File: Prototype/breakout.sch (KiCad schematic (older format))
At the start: 8 parts, among them J2 Conn_02x03_Counter_Clockwise, Q1 BSC026NE2LS5, U1 INA214, U2 bq297xx, U3 LM21215, U4 TPS61088, U5 ADA4891-4

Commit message: Test
hello
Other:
- note added: "hello"
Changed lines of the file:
@@
 Wire Wire Line
 	1700 4100 1900 4100
+Text Notes 1700 4800 0    60   ~ 0
+hello
 $EndSCHEMATC

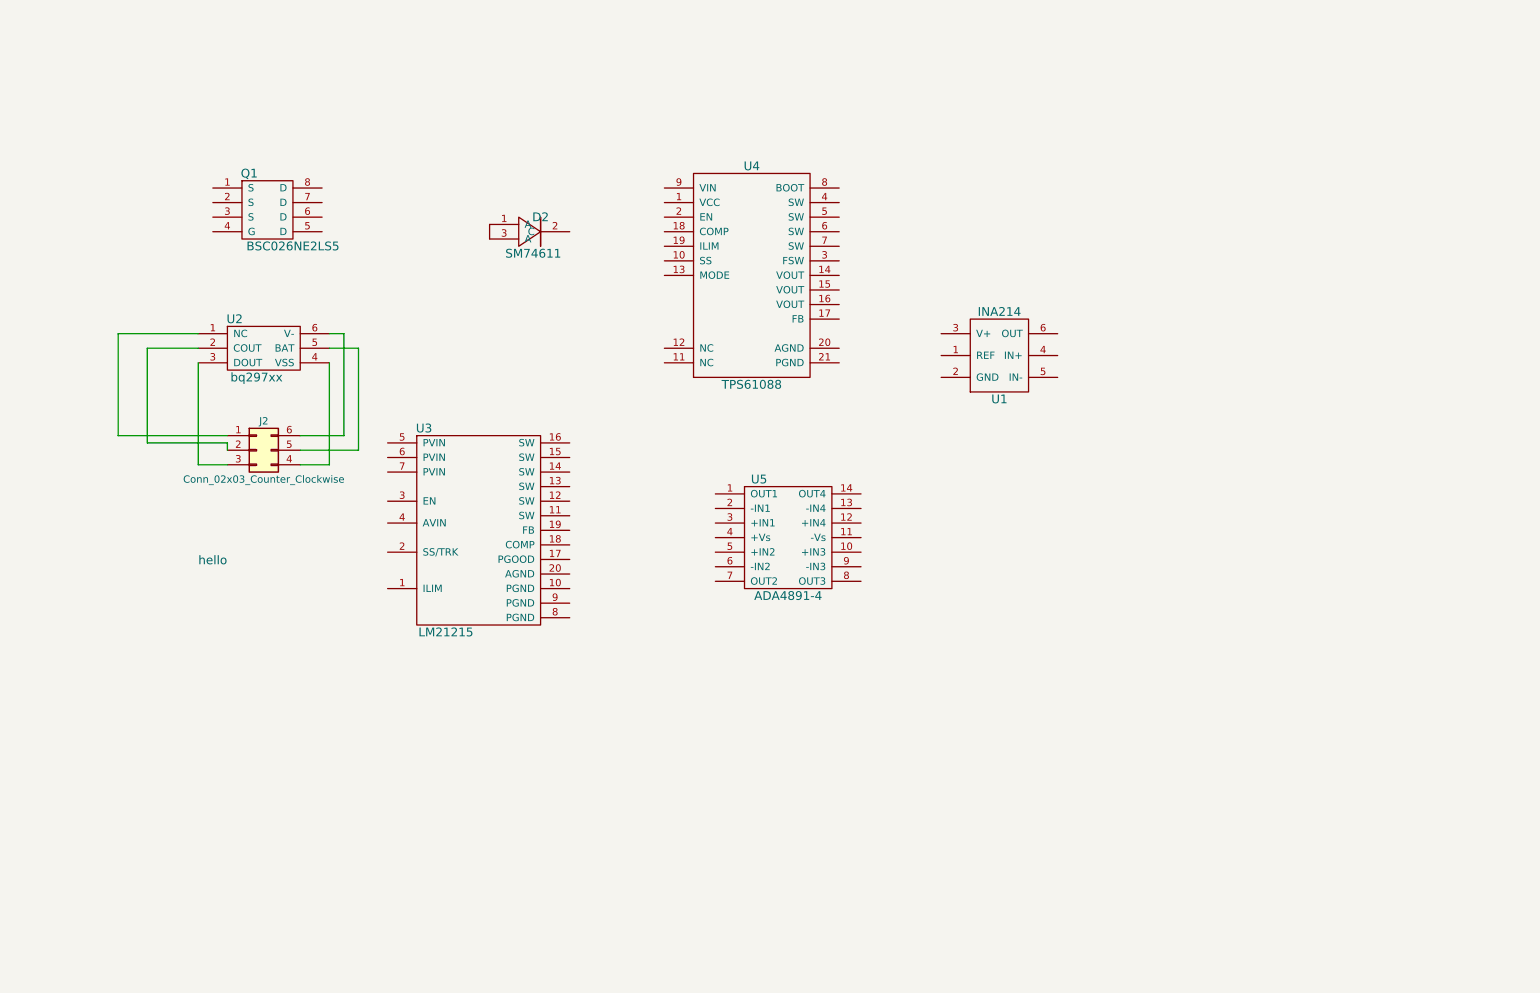
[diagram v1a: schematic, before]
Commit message: Finished laying out breakout boards
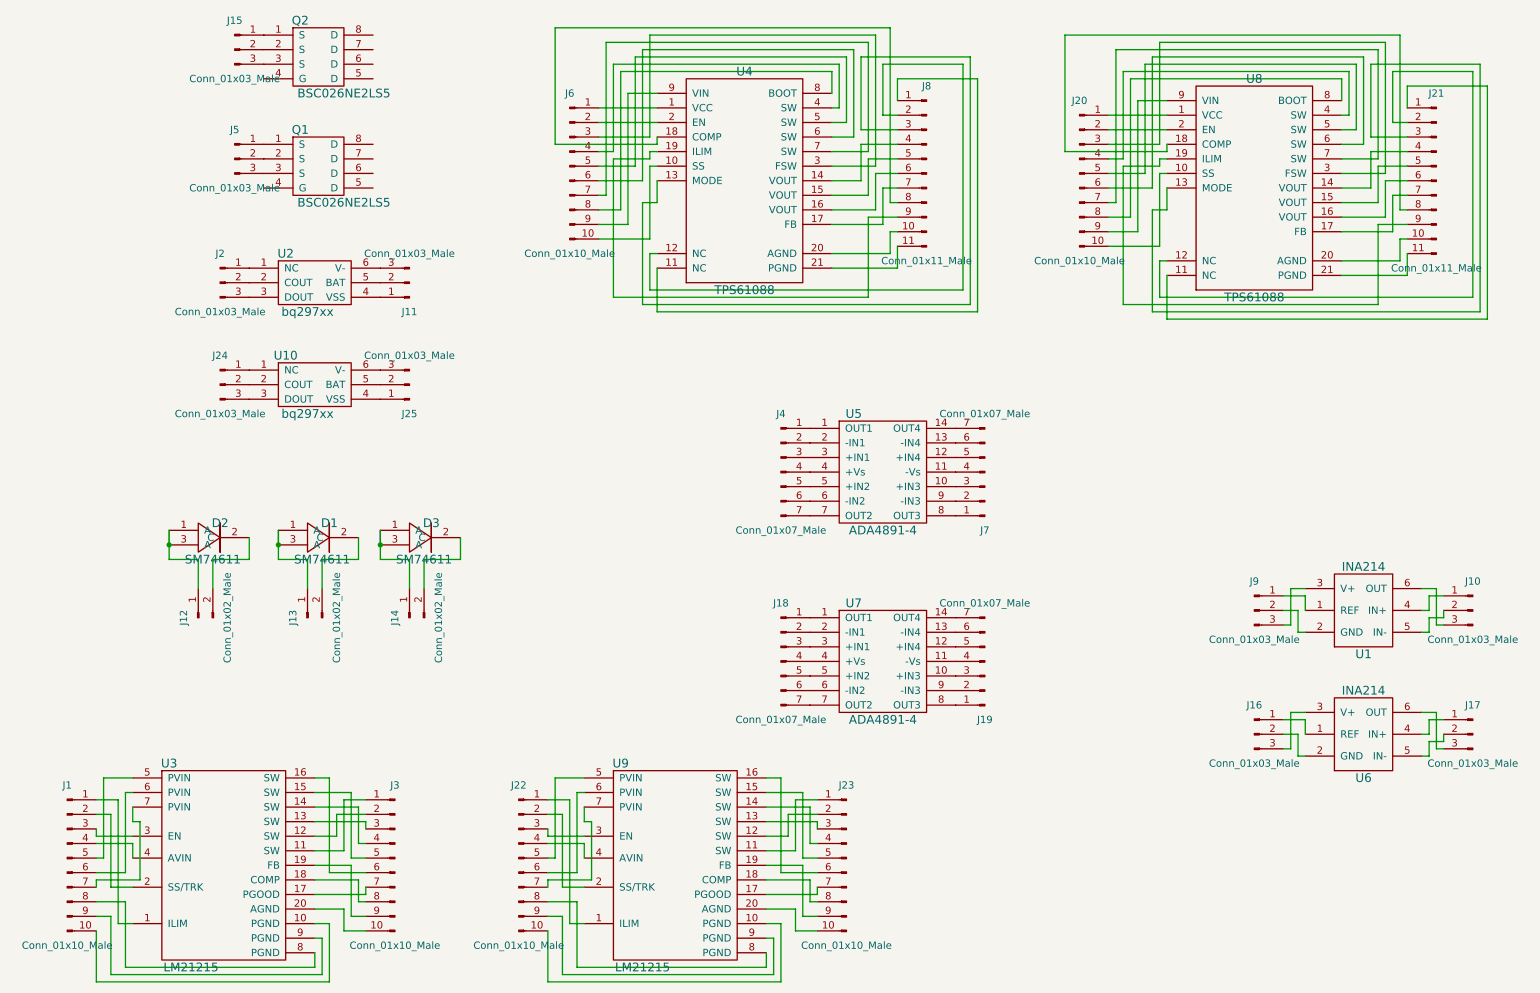
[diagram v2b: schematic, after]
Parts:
- removed J2: Conn_02x03_Counter_Clockwise, Pin_Headers:Pin_Header_Straight_2x03_Pitch2.54mm, symbol Conn_02x03_Counter_Clockwise
- added D1, D3: SM74611, Diodes_SMD:DD-PAK_TO263_SingleDiode, symbol SM74611
- added J1, J20, J22, J23, J3, J6: Conn_01x10_Male, Pin_Headers:Pin_Header_Straight_1x10_Pitch2.54mm, symbol Conn_01x10_Male
- added J10, J11, J15, J16, J17, J2, J24, J25, J5, J9: Conn_01x03_Male, Pin_Headers:Pin_Header_Straight_1x03_Pitch2.54mm, symbol Conn_01x03_Male
- added J12, J13, J14: Conn_01x02_Male, Pin_Headers:Pin_Header_Straight_1x02_Pitch2.54mm, symbol Conn_01x02_Male
- added J18, J19, J4, J7: Conn_01x07_Male, Pin_Headers:Pin_Header_Straight_1x07_Pitch2.54mm, symbol Conn_01x07_Male
- added J21, J8: Conn_01x11_Male, Pin_Headers:Pin_Header_Straight_1x11_Pitch2.54mm, symbol Conn_01x11_Male
- added Q2: BSC026NE2LS5, Housings_SON:VSONP-8-1EP_5x6_Pitch1.27mm, symbol BSC026NE2LS5
- added U10: bq297xx, Housings_SON:WSON6_1.5x1.5mm_Pitch0.5mm, symbol bq297xx
- added U6: INA214, kicad-libraries:SC70-6, symbol INA214
- added U7: ADA4891-4, SMD_Packages:SSOP-14, symbol ADA4891-4
- added U8: TPS61088, Housings_DFN_QFN:Texas_VQFN-RGR-20, symbol TPS61088
- added U9: LM21215, SMD_Packages:SSOP-20, symbol LM21215
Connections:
- net at U1.1 (REF): now also J9.1 (Pin_1)
- net at U1.2 (GND): now also J9.2 (Pin_2)
- net at U1.3 (V+): now also J9.3 (Pin_3)
- net at U1.4 (IN+): now also J10.1 (Pin_1)
- net at U1.5 (IN-): now also J10.2 (Pin_2)
- net at U1.6 (OUT): now also J10.3 (Pin_3)
- net at D2.1 (A): now also D2.3 (A), J12.1 (Pin_1)
- net at D2.2 (C): now also J12.2 (Pin_2)
- net at U4.1 (VCC): now also J6.1 (Pin_1)
- net at U4.10 (SS): now also J6.10 (Pin_10)
- net at U4.11 (NC): now also J8.1 (Pin_1)
- net at U4.12 (NC): now also J8.2 (Pin_2)
- net at U4.13 (MODE): now also J8.3 (Pin_3)
- net at U4.14 (VOUT): now also J8.4 (Pin_4)
- net at U4.15 (VOUT): now also J8.5 (Pin_5)
- net at U4.16 (VOUT): now also J8.6 (Pin_6)
- net at U4.17 (FB): now also J8.7 (Pin_7)
- net at U4.18 (COMP): now also J8.8 (Pin_8)
- net at U4.19 (ILIM): now also J8.9 (Pin_9)
- net at U4.2 (EN): now also J6.2 (Pin_2)
- net at U4.20 (AGND): now also J8.10 (Pin_10)
- net at U4.21 (PGND): now also J8.11 (Pin_11)
- net at U4.3 (FSW): now also J6.3 (Pin_3)
- net at U4.4 (SW): now also J6.4 (Pin_4)
- net at U4.5 (SW): now also J6.5 (Pin_5)
- net at U4.6 (SW): now also J6.6 (Pin_6)
- net at U4.7 (SW): now also J6.7 (Pin_7)
- net at U4.8 (BOOT): now also J6.8 (Pin_8)
- net at U4.9 (VIN): now also J6.9 (Pin_9)
- net at Q1.1 (S): now also J5.1 (Pin_1)
- net at Q1.2 (S): now also J5.2 (Pin_2)
- net at Q1.3 (S): now also J5.3 (Pin_3)
- net at U2.1 (NC): now also J2.1 (Pin_1)
- net at U2.2 (COUT): now also J2.2 (Pin_2)
- net at U2.3 (DOUT): now also J2.3 (Pin_3)
- net at U2.4 (VSS): now also J11.1 (Pin_1)
- net at U2.5 (BAT): now also J11.2 (Pin_2)
- net at U2.6 (V-): now also J11.3 (Pin_3)
- net at U3.1 (ILIM): now also J1.1 (Pin_1)
- net at U3.10 (PGND): now also J1.10 (Pin_10)
- net at U3.11 (SW): now also J3.1 (Pin_1)
- net at U3.12 (SW): now also J3.2 (Pin_2)
- net at U3.13 (SW): now also J3.3 (Pin_3)
- net at U3.14 (SW): now also J3.4 (Pin_4)
- net at U3.15 (SW): now also J3.5 (Pin_5)
- net at U3.16 (SW): now also J3.6 (Pin_6)
- net at U3.17 (PGOOD): now also J3.7 (Pin_7)
- net at U3.18 (COMP): now also J3.8 (Pin_8)
- net at U3.19 (FB): now also J3.9 (Pin_9)
- net at U3.2 (SS/TRK): now also J1.2 (Pin_2)
- net at U3.20 (AGND): now also J3.10 (Pin_10)
- net at U3.3 (EN): now also J1.3 (Pin_3)
- net at U3.4 (AVIN): now also J1.4 (Pin_4)
- net at U3.5 (PVIN): now also J1.5 (Pin_5)
- net at U3.6 (PVIN): now also J1.6 (Pin_6)
- net at U3.7 (PVIN): now also J1.7 (Pin_7)
- net at U3.8 (PGND): now also J1.8 (Pin_8)
- net at U3.9 (PGND): now also J1.9 (Pin_9)
- net at U5.1 (OUT1): now also J4.1 (Pin_1)
- net at U5.10 (+IN3): now also J7.3 (Pin_3)
- net at U5.11 (-Vs): now also J7.4 (Pin_4)
- net at U5.12 (+IN4): now also J7.5 (Pin_5)
- net at U5.13 (-IN4): now also J7.6 (Pin_6)
- net at U5.14 (OUT4): now also J7.7 (Pin_7)
- net at U5.2 (-IN1): now also J4.2 (Pin_2)
- net at U5.3 (+IN1): now also J4.3 (Pin_3)
- net at U5.4 (+Vs): now also J4.4 (Pin_4)
- net at U5.5 (+IN2): now also J4.5 (Pin_5)
- net at U5.6 (-IN2): now also J4.6 (Pin_6)
- net at U5.7 (OUT2): now also J4.7 (Pin_7)
- net at U5.8 (OUT3): now also J7.1 (Pin_1)
- net at U5.9 (-IN3): now also J7.2 (Pin_2)
- new net: D1.1 (A), D1.3 (A), J13.1 (Pin_1)
- new net: D1.2 (C), J13.2 (Pin_2)
- new net: D3.1 (A), D3.3 (A), J14.1 (Pin_1)
- new net: D3.2 (C), J14.2 (Pin_2)
- new net: J15.1 (Pin_1), Q2.1 (S)
- new net: J15.2 (Pin_2), Q2.2 (S)
- new net: J15.3 (Pin_3), Q2.3 (S)
- new net: J16.1 (Pin_1), U6.1 (REF)
- new net: J16.2 (Pin_2), U6.2 (GND)
- new net: J16.3 (Pin_3), U6.3 (V+)
- new net: J17.1 (Pin_1), U6.4 (IN+)
- new net: J17.2 (Pin_2), U6.5 (IN-)
- new net: J17.3 (Pin_3), U6.6 (OUT)
- new net: J18.1 (Pin_1), U7.1 (OUT1)
- new net: J19.3 (Pin_3), U7.10 (+IN3)
- new net: J19.4 (Pin_4), U7.11 (-Vs)
- new net: J19.5 (Pin_5), U7.12 (+IN4)
- new net: J19.6 (Pin_6), U7.13 (-IN4)
- new net: J19.7 (Pin_7), U7.14 (OUT4)
- new net: J18.2 (Pin_2), U7.2 (-IN1)
- new net: J18.3 (Pin_3), U7.3 (+IN1)
- new net: J18.4 (Pin_4), U7.4 (+Vs)
- new net: J18.5 (Pin_5), U7.5 (+IN2)
- new net: J18.6 (Pin_6), U7.6 (-IN2)
- new net: J18.7 (Pin_7), U7.7 (OUT2)
- new net: J19.1 (Pin_1), U7.8 (OUT3)
- new net: J19.2 (Pin_2), U7.9 (-IN3)
- new net: J20.1 (Pin_1), U8.1 (VCC)
- new net: J20.10 (Pin_10), U8.10 (SS)
- new net: J21.1 (Pin_1), U8.11 (NC)
- new net: J21.2 (Pin_2), U8.12 (NC)
- new net: J21.3 (Pin_3), U8.13 (MODE)
- new net: J21.4 (Pin_4), U8.14 (VOUT)
- new net: J21.5 (Pin_5), U8.15 (VOUT)
- new net: J21.6 (Pin_6), U8.16 (VOUT)
- new net: J21.7 (Pin_7), U8.17 (FB)
- new net: J21.8 (Pin_8), U8.18 (COMP)
- new net: J21.9 (Pin_9), U8.19 (ILIM)
- new net: J20.2 (Pin_2), U8.2 (EN)
- new net: J21.10 (Pin_10), U8.20 (AGND)
- new net: J21.11 (Pin_11), U8.21 (PGND)
- new net: J20.3 (Pin_3), U8.3 (FSW)
- new net: J20.4 (Pin_4), U8.4 (SW)
- new net: J20.5 (Pin_5), U8.5 (SW)
- new net: J20.6 (Pin_6), U8.6 (SW)
- new net: J20.7 (Pin_7), U8.7 (SW)
- new net: J20.8 (Pin_8), U8.8 (BOOT)
- new net: J20.9 (Pin_9), U8.9 (VIN)
- new net: J22.1 (Pin_1), U9.1 (ILIM)
- new net: J22.10 (Pin_10), U9.10 (PGND)
- new net: J22.2 (Pin_2), U9.2 (SS/TRK)
- new net: J22.3 (Pin_3), U9.3 (EN)
- new net: J22.4 (Pin_4), U9.4 (AVIN)
- new net: J22.5 (Pin_5), U9.5 (PVIN)
- new net: J22.6 (Pin_6), U9.6 (PVIN)
- new net: J22.7 (Pin_7), U9.7 (PVIN)
- new net: J22.8 (Pin_8), U9.8 (PGND)
- new net: J22.9 (Pin_9), U9.9 (PGND)
- new net: J23.1 (Pin_1), U9.11 (SW)
- new net: J23.10 (Pin_10), U9.20 (AGND)
- new net: J23.2 (Pin_2), U9.12 (SW)
- new net: J23.3 (Pin_3), U9.13 (SW)
- new net: J23.4 (Pin_4), U9.14 (SW)
- new net: J23.5 (Pin_5), U9.15 (SW)
- new net: J23.6 (Pin_6), U9.16 (SW)
- new net: J23.7 (Pin_7), U9.17 (PGOOD)
- new net: J23.8 (Pin_8), U9.18 (COMP)
- new net: J23.9 (Pin_9), U9.19 (FB)
- new net: J24.1 (Pin_1), U10.1 (NC)
- new net: J24.2 (Pin_2), U10.2 (COUT)
- new net: J24.3 (Pin_3), U10.3 (DOUT)
- new net: J25.1 (Pin_1), U10.4 (VSS)
- new net: J25.2 (Pin_2), U10.5 (BAT)
- new net: J25.3 (Pin_3), U10.6 (V-)
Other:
- note removed: "hello"
- moved on the sheet: D2, Q1, U1, U2, U3, U4, U5

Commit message: Changed footprint of TPS61088
Also added a dot beside pin 1 of INA214
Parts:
- U4, U8: footprint Housings_DFN_QFN:Texas_VQFN-RGR-20 -> w_smd_qfn:pvqfn-n20
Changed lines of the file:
@@
 F 0 "U4" H 5450 2900 60  0000 C CNN
 F 1 "TPS61088" H 5450 1400 60  0000 C CNN
-F 2 "Housings_DFN_QFN:Texas_VQFN-RGR-20" H 5450 1850 60  0001 C CNN
+F 2 "w_smd_qfn:pvqfn-n20" H 5450 1850 60  0001 C CNN
 F 3 "" H 5450 1850 60  0001 C CNN
 	1    5450 2150
@@
 F 0 "U8" H 8950 2950 60  0000 C CNN
 F 1 "TPS61088" H 8950 1450 60  0000 C CNN
-F 2 "Housings_DFN_QFN:Texas_VQFN-RGR-20" H 8950 1900 60  0001 C CNN
+F 2 "w_smd_qfn:pvqfn-n20" H 8950 1900 60  0001 C CNN
 F 3 "" H 8950 1900 60  0001 C CNN
 	1    8950 2200
